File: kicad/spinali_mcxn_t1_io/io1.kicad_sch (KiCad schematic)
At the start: 33 parts, among them J10 SPI2, J3 I2C1, J4 I2C2, J5 UART1, J6 UART2, J7 QDEC, J9 SPI1

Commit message: Finished IO board layout positioning. Started routing.
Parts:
- J10, J9: footprint Connector_JST:JST_GH_SM07B-GHS-TB_1x07-1MP_P1.25mm_Horizontal -> Connector_JST:JST_GH_BM07B-GHS-TBT_1x07-1MP_P1.25mm_Vertical
- J3, J4: footprint Connector_JST:JST_GH_SM04B-GHS-TB_1x04-1MP_P1.25mm_Horizontal -> Connector_JST:JST_GH_BM04B-GHS-TBT_1x04-1MP_P1.25mm_Vertical
- J5, J6, J7: footprint Connector_JST:JST_GH_SM06B-GHS-TB_1x06-1MP_P1.25mm_Horizontal -> Connector_JST:JST_GH_BM06B-GHS-TBT_1x06-1MP_P1.25mm_Vertical
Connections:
- net at D2.5 (IO_4): now also D2.6 (NC_1)
- net at D1.5 (IO_4): now also D1.6 (NC_1)
- net at D4.4 (IO_3): now also D4.7 (NC_2)
- net at D4.5 (IO_4): now also D4.6 (NC_1)
- net at D6.4 (IO_3): now also D6.7 (NC_2)
- net at D6.5 (IO_4): now also D6.6 (NC_1)
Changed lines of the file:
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@@
 			)
 		)
-		(property "Footprint" "Connector_JST:JST_GH_SM06B-GHS-TB_1x06-1MP_P1.25mm_Horizontal"
+		(property "Footprint" "Connector_JST:JST_GH_BM06B-GHS-TBT_1x06-1MP_P1.25mm_Vertical"
 			(at 377.19 85.852 0)
 			(effects
@@
 			)
 		)
-		(property "Footprint" "Connector_JST:JST_GH_SM04B-GHS-TB_1x04-1MP_P1.25mm_Horizontal"
+		(property "Footprint" "Connector_JST:JST_GH_BM04B-GHS-TBT_1x04-1MP_P1.25mm_Vertical"
 			(at 171.45 112.522 0)
 			(effects
@@
 			)
 		)
-		(property "Footprint" "Connector_JST:JST_GH_SM04B-GHS-TB_1x04-1MP_P1.25mm_Horizontal"
+		(property "Footprint" "Connector_JST:JST_GH_BM04B-GHS-TBT_1x04-1MP_P1.25mm_Vertical"
 			(at 171.45 73.152 0)
 			(effects
@@
 			)
 		)
-		(property "Footprint" "Connector_JST:JST_GH_SM06B-GHS-TB_1x06-1MP_P1.25mm_Horizontal"
+		(property "Footprint" "Connector_JST:JST_GH_BM06B-GHS-TBT_1x06-1MP_P1.25mm_Vertical"
 			(at 377.19 178.562 0)
 			(effects
@@
 			)
 		)
-		(property "Footprint" "Connector_JST:JST_GH_SM07B-GHS-TB_1x07-1MP_P1.25mm_Horizontal"
+		(property "Footprint" "Connector_JST:JST_GH_BM07B-GHS-TBT_1x07-1MP_P1.25mm_Vertical"
 			(at 171.45 177.292 0)
 			(effects
@@
 			)
 		)
-		(property "Footprint" "Connector_JST:JST_GH_SM07B-GHS-TB_1x07-1MP_P1.25mm_Horizontal"
+		(property "Footprint" "Connector_JST:JST_GH_BM07B-GHS-TBT_1x07-1MP_P1.25mm_Vertical"
 			(at 171.45 254.762 0)
 			(effects
@@
 			)
 		)
-		(property "Footprint" "Connector_JST:JST_GH_SM06B-GHS-TB_1x06-1MP_P1.25mm_Horizontal"
+		(property "Footprint" "Connector_JST:JST_GH_BM06B-GHS-TBT_1x06-1MP_P1.25mm_Vertical"
 			(at 377.19 134.112 0)
 			(effects

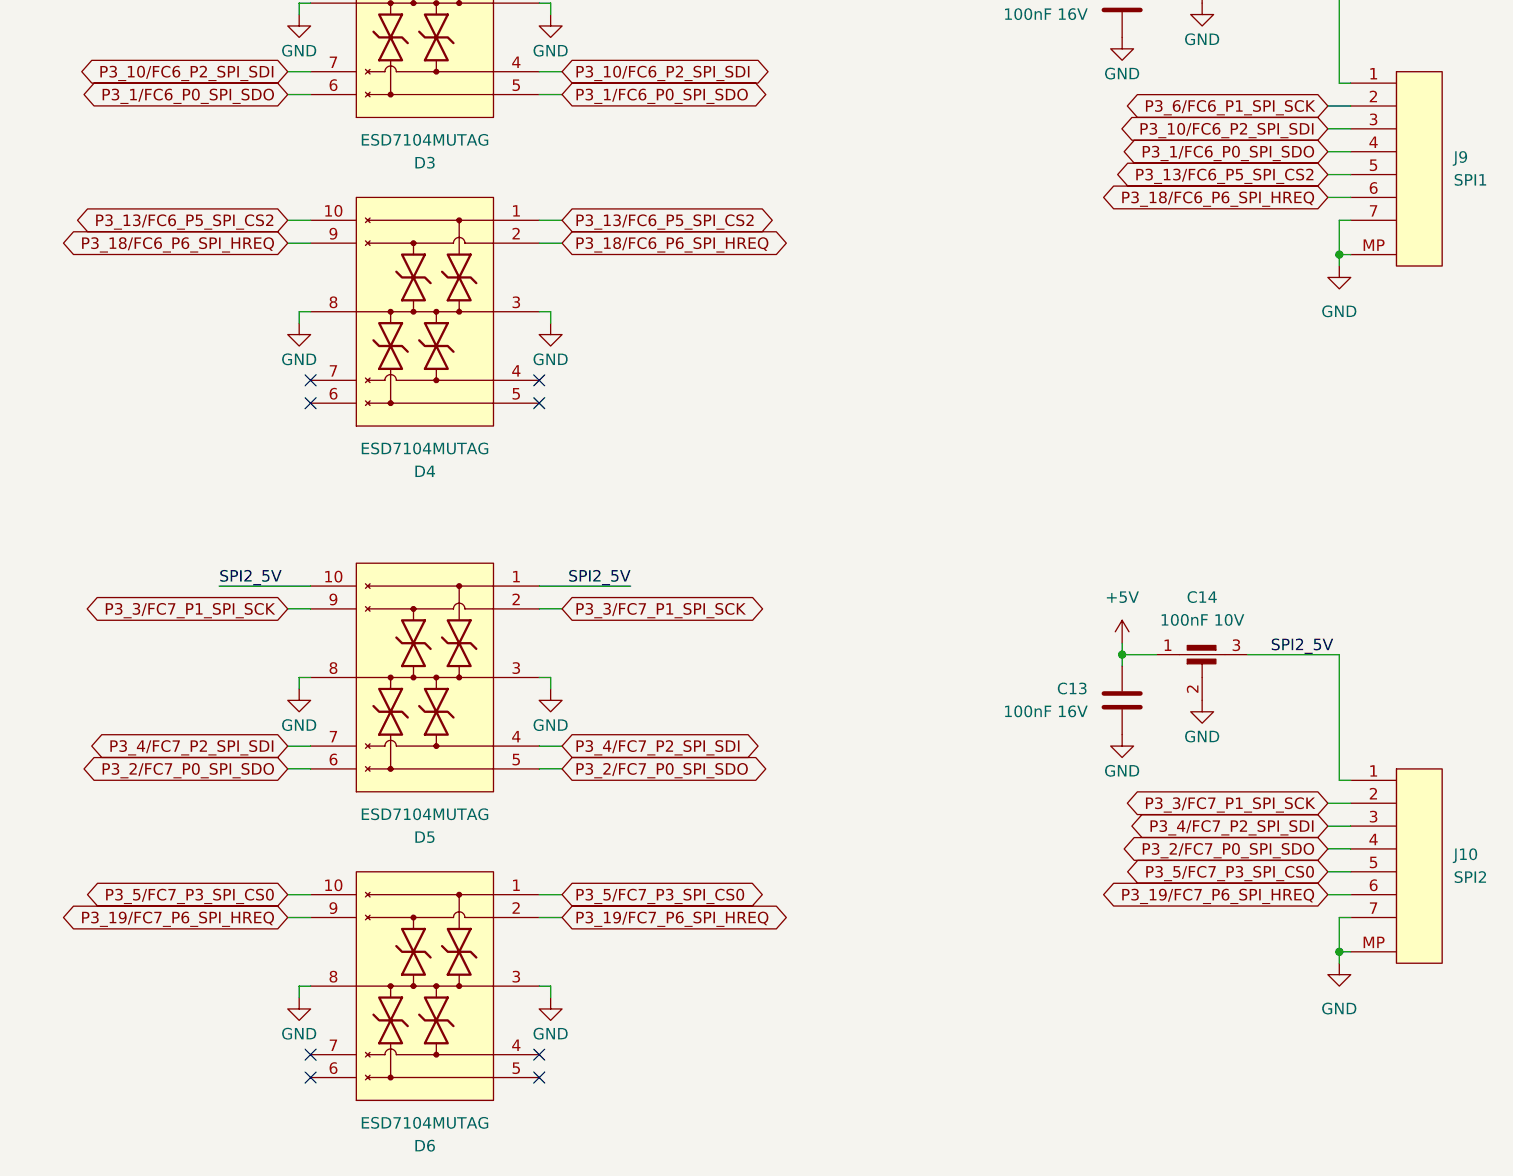
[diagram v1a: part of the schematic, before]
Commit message: Updated schematic and layout after review (ready for production)
- Replaced TVS diode at ESC1 and ESC2 connector with higher voltage one.
- Replaced MUTAG7104 TVS with single TVS at some places to reduce cost.
- Added 1k5 pull-down resistor on GPS safety switch.
- Generated all production files.
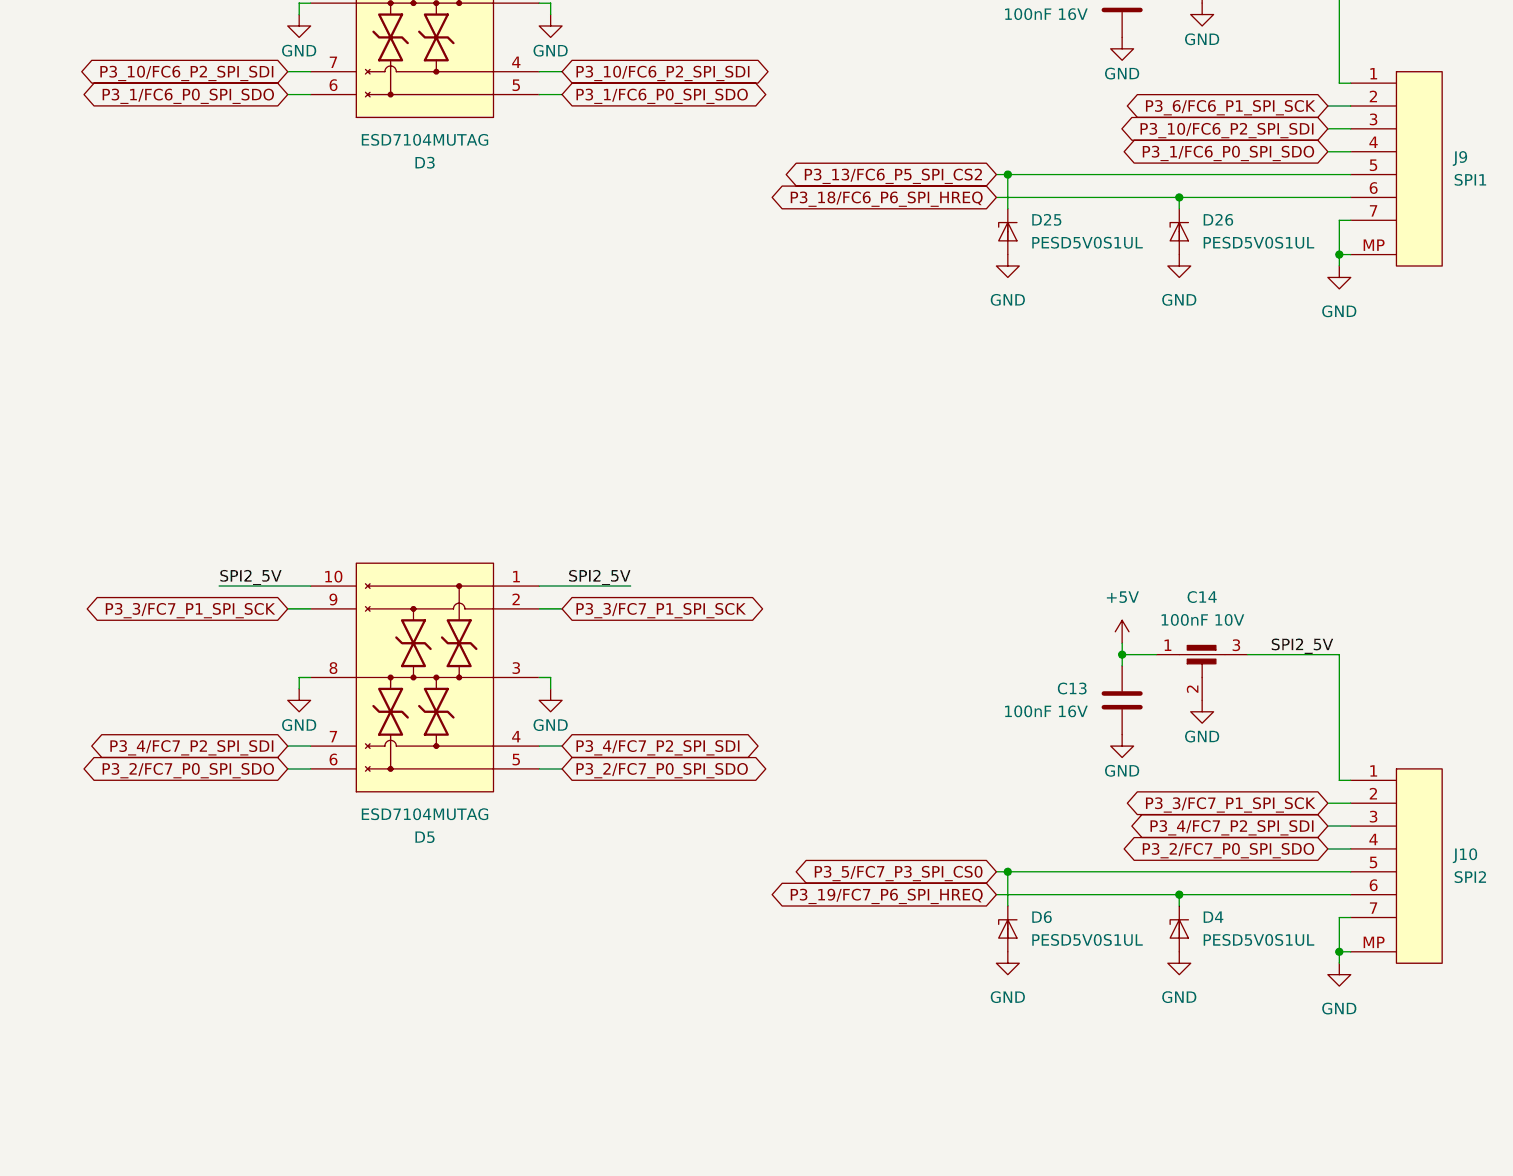
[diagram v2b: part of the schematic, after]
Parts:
- removed D4, D6: ESD7104MUTAG, TVS:ESD8104MUTAG, symbol TVS:ESD7104MUTAG
- added D25, D26, D4, D6: PESD5V0S1UL, TVS:PESD5V0S1ULD315, symbol TVS:PESD5V0S1UL
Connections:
- net GND: now also D25.2 (A), D26.2 (A), D4.2 (A), D6.2 (A)
- net P3_13/FC6_P5_SPI_CS2: now also D25.1 (K1)
- net P3_18/FC6_P6_SPI_HREQ: now also D26.1 (K1)
- net P3_19/FC7_P6_SPI_HREQ: now also D4.1 (K1)
- net P3_5/FC7_P3_SPI_CS0: now also D6.1 (K1)
- net at D2.5 (IO_4): now also D2.6 (NC_1)
- net at D1.5 (IO_4): now also D1.6 (NC_1)
- no-connect marks 12 -> 4

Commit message: Updated MCXN-T1 IO board
- Fixed that JST GH connectors are now the correct part number.
- Updated silkscreen positioning.
- Generated production files for Eurocircuits (global) and JLCPCB
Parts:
- J10, J9: DigiKey 455-1569-1-ND -> 455-BM07B-GHS-TBTCT-ND; MFPN SM07B-GHS-TB -> BM07B-GHS-TBT
- J3, J4: DigiKey 455-1566-1-ND -> 455-BM04B-GHS-TBTCT-ND; MFPN SM04B-GHS-TB -> BM04B-GHS-TBT
- J5, J6, J7: DigiKey 455-1568-1-ND -> 455-BM06B-GHS-TBTCT-ND; MFPN SM06B-GHS-TB -> BM06B-GHS-TBT
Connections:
- net at D2.5 (IO_4): now also D2.6 (NC_1)
- net at D1.5 (IO_4): now also D1.6 (NC_1)
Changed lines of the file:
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@@
 			)
 		)
-		(property "MFPN" "SM06B-GHS-TB"
+		(property "MFPN" "BM06B-GHS-TBT"
 			(at 377.19 90.424 0)
 			(effects
@@
 			)
 		)
-		(property "DigiKey" "455-1568-1-ND"
+		(property "DigiKey" "455-BM06B-GHS-TBTCT-ND"
 			(at 377.19 92.71 0)
 			(effects
@@
 			)
 		)
-		(property "MFPN" "SM04B-GHS-TB"
+		(property "MFPN" "BM04B-GHS-TBT"
 			(at 171.45 116.586 0)
 			(effects
@@
 			)
 		)
-		(property "DigiKey" "455-1566-1-ND"
+		(property "DigiKey" "455-BM04B-GHS-TBTCT-ND"
 			(at 171.45 118.618 0)
 			(effects
@@
 			)
 		)
-		(property "MFPN" "SM04B-GHS-TB"
+		(property "MFPN" "BM04B-GHS-TBT"
 			(at 171.45 77.216 0)
 			(effects
@@
 			)
 		)
-		(property "DigiKey" "455-1566-1-ND"
+		(property "DigiKey" "455-BM04B-GHS-TBTCT-ND"
 			(at 171.45 79.248 0)
 			(effects
@@
 			)
 		)
-		(property "MFPN" "SM06B-GHS-TB"
+		(property "MFPN" "BM06B-GHS-TBT"
 			(at 377.19 183.134 0)
 			(effects
@@
 			)
 		)
-		(property "DigiKey" "455-1568-1-ND"
+		(property "DigiKey" "455-BM06B-GHS-TBTCT-ND"
 			(at 377.19 185.42 0)
 			(effects
@@
 			)
 		)
-		(property "MFPN" "SM07B-GHS-TB"
+		(property "MFPN" "BM07B-GHS-TBT"
 			(at 171.45 181.864 0)
 			(effects
@@
 			)
 		)
-		(property "DigiKey" "455-1569-1-ND"
+		(property "DigiKey" "455-BM07B-GHS-TBTCT-ND"
 			(at 171.45 184.15 0)
 			(effects
@@
 			)
 		)
-		(property "MFPN" "SM07B-GHS-TB"
+		(property "MFPN" "BM07B-GHS-TBT"
 			(at 171.45 259.334 0)
 			(effects
@@
 			)
 		)
-		(property "DigiKey" "455-1569-1-ND"
+		(property "DigiKey" "455-BM07B-GHS-TBTCT-ND"
 			(at 171.45 261.62 0)
 			(effects
@@
 			)
 		)
-		(property "MFPN" "SM06B-GHS-TB"
+		(property "MFPN" "BM06B-GHS-TBT"
 			(at 377.19 138.684 0)
 			(effects
@@
 			)
 		)
-		(property "DigiKey" "455-1568-1-ND"
+		(property "DigiKey" "455-BM06B-GHS-TBTCT-ND"
 			(at 377.19 140.97 0)
 			(effects
